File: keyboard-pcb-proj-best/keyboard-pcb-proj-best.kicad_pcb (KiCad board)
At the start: 2 copper layers, 24 parts, among them SW1 SW_PUSH, U1 ATmega32U4-A, Y1 16Mhz

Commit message: pcb routing
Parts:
- moved C4 1.73 mm to (94.0, 91.0)
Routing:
- net GND: track 65.5 -> 197.5 mm, vias 0 -> 2
- net +5V: track 44.0 -> 110.0 mm, vias 0 -> 7
- net ROW0: track 0.00 -> 20.4 mm
- net ROW1: track 0.00 -> 19.7 mm
- net COL1: track 0.00 -> 19.1 mm
- net COL0: track 0.00 -> 19.1 mm
- net Net-(D1-A): track 0.00 -> 7.17 mm
- net Net-(D2-A): track 0.00 -> 7.07 mm
- net Net-(D4-A): track 0.00 -> 7.00 mm
- net Net-(D3-A): track 0.00 -> 7.00 mm
- net Net-(U1-~{HWB}/PE2): track 0.00 -> 4.75 mm

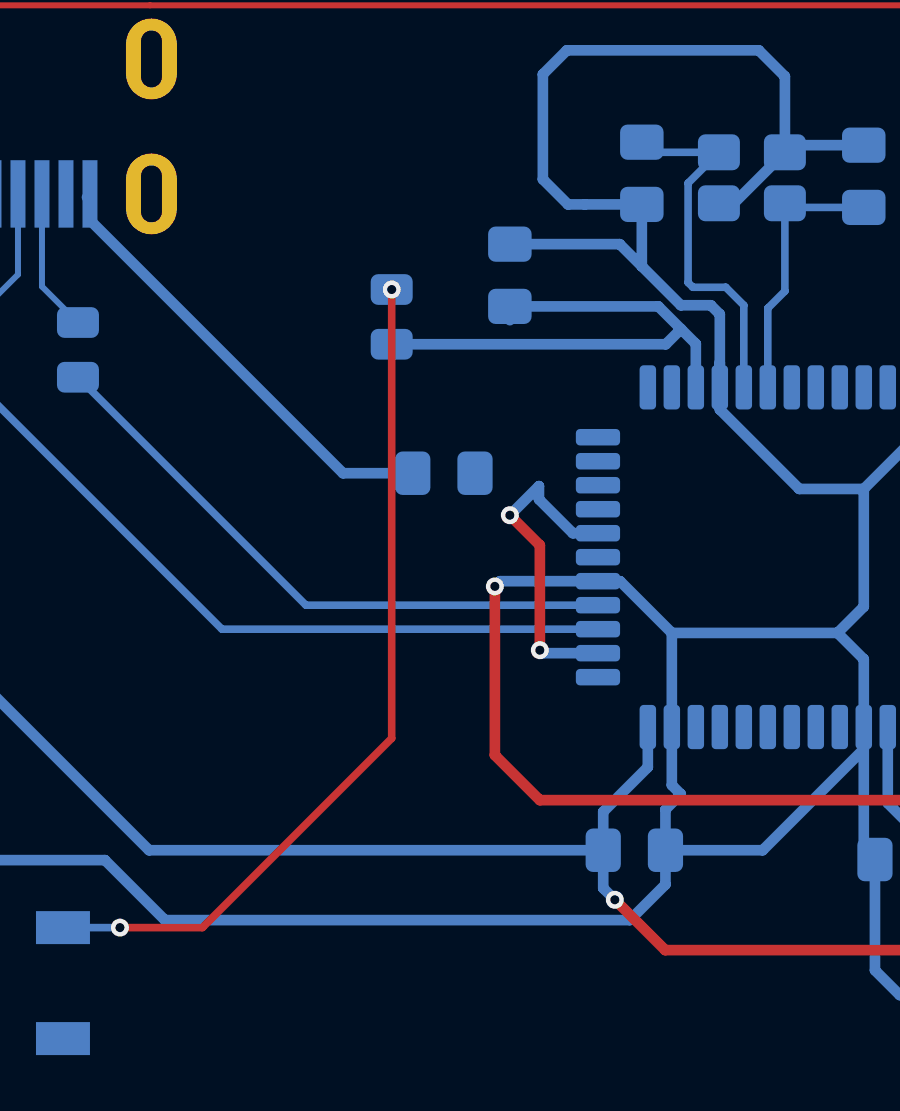
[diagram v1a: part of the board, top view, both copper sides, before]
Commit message: Finished Routing
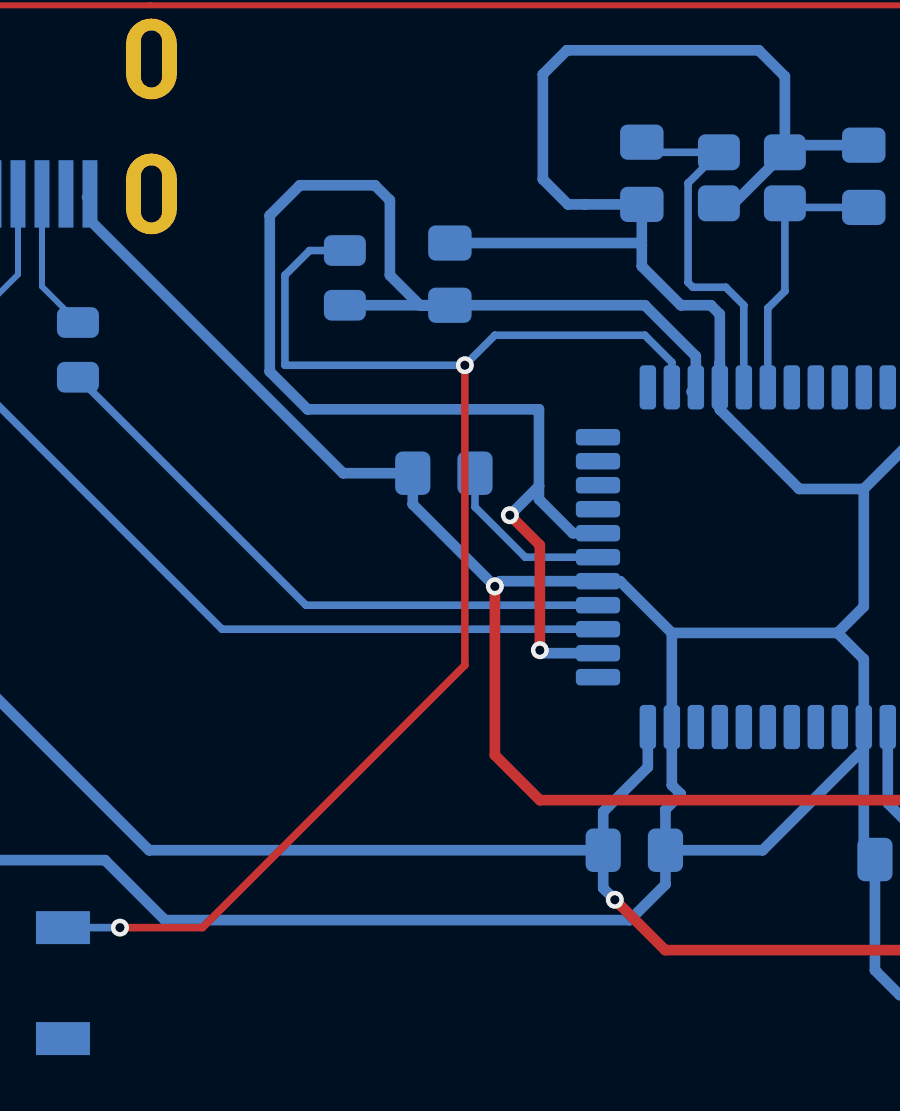
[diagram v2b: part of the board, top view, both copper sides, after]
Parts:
- moved R4 2.03 mm to (88.5, 91.1)
- moved C4 2.00 mm to (92.0, 91.0)
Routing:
- net +5V: track 110.0 -> 132.0 mm
- net Net-(U1-~{RESET}): track 29.1 -> 47.5 mm
- net GND: track 197.5 -> 204.1 mm
- net Net-(U1-UCAP): track 0.00 -> 5.92 mm
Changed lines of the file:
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@@
 	(footprint "Capacitor_SMD:C_0805_2012Metric_Pad1.18x1.45mm_HandSolder"
 		(layer "B.Cu")
-		(at 94 91 90)
+		(at 92 90.9625 90)
 		(descr "Capacitor SMD 0805 (2012 Metric), square (rectangular) end terminal, IPC-7351 nominal with elongated pad for handsoldering. (Body size source: IPC-SM-782 page 76, https://www.pcb-3d.com/wordpress/wp-content/uploads/ipc-sm-782a_amendment_1_and_2.pdf, https://docs.google.com/spreadsheets/d/1BsfQQcO9C6DZCsRaXUlFlo91Tg2WpOkGARC1WS5S8t0/edit?usp=sharing), generated with kicad-footprint-generator")
 		(tags "capacitor handsolder")
@@
 	(footprint "Resistor_SMD:R_0805_2012Metric"
 		(layer "B.Cu")
-		(at 90.06 92.3875 90)
+		(at 88.5 91.0875 90)
 		(descr "Resistor SMD 0805 (2012 Metric), square (rectangular) end terminal, IPC-7351 nominal, (Body size source: IPC-SM-782 page 72, https://www.pcb-3d.com/wordpress/wp-content/uploads/ipc-sm-782a_amendment_1_and_2.pdf), generated with kicad-footprint-generator")
 		(tags "resistor")
@@
 	)
 	(segment
+		(start 94.511873 100.4)
+		(end 96.9375 100.4)
+		(width 0.254)
+		(layer "B.Cu")
+		(net 1)
+	)
+	(segment
+		(start 92.8375 97.6)
+		(end 92.8375 98.725627)
+		(width 0.254)
+		(layer "B.Cu")
+		(net 1)
+	)
+	(segment
+		(start 92.8375 98.725627)
+		(end 94.511873 100.4)
+		(width 0.254)
+		(layer "B.Cu")
+		(net 1)
+	)
+	(segment
 		(start 93.5 107)
 		(end 95 108.5)
@@
 	)
 	(segment
+		(start 98.325 89.925)
+		(end 98.4 90)
+		(width 0.3556)
+		(layer "B.Cu")
+		(net 2)
+	)
+	(segment
 		(start 105.8 110.1075)
 		(end 105.8 106.0625)
@@
 	)
 	(segment
-		(start 97.6625 89.9625)
-		(end 98.4 90.7)
-		(width 0.3556)
-		(layer "B.Cu")
-		(net 2)
-	)
-	(segment
 		(start 99.7 92)
 		(end 100.7 92)
@@
 	)
 	(segment
+		(start 110.7625 96.4)
+		(end 108.2625 96.4)
+		(width 0.3556)
+		(layer "B.Cu")
+		(net 2)
+	)
+	(segment
 		(start 97.674999 101.2)
 		(end 96.9375 101.2)
@@
 	)
 	(segment
-		(start 112.91 94.2525)
-		(end 110.7625 96.4)
-		(width 0.3556)
-		(layer "B.Cu")
-		(net 2)
-	)
-	(segment
 		(start 98.4 90.7)
 		(end 99.7 92)
@@
 	)
 	(segment
-		(start 94 89.9625)
-		(end 97.6625 89.9625)
+		(start 90.7625 98.6355)
+		(end 93.5 101.373)
 		(width 0.3556)
 		(layer "B.Cu")
@@
 	)
 	(segment
-		(start 110.7625 96.4)
-		(end 108.2625 96.4)
-		(width 0.3556)
-		(layer "B.Cu")
-		(net 2)
-	)
-	(segment
 		(start 99.7 108.3)
 		(end 99.4 108)
@@
 	)
 	(segment
+		(start 90.7625 97.6)
+		(end 90.7625 98.6355)
+		(width 0.3556)
+		(layer "B.Cu")
+		(net 2)
+	)
+	(segment
 		(start 112.8 114.2)
 		(end 112.8 105.7125)
@@
 	)
 	(segment
+		(start 112.91 94.2525)
+		(end 110.7625 96.4)
+		(width 0.3556)
+		(layer "B.Cu")
+		(net 2)
+	)
+	(segment
 		(start 102.3 83.5)
 		(end 103.17 84.37)
@@
 	)
 	(segment
+		(start 98.4 90)
+		(end 98.4 90.7)
+		(width 0.3556)
+		(layer "B.Cu")
+		(net 2)
+	)
+	(segment
 		(start 72.9 116.45)
 		(end 71.45 116.45)
@@
 	)
 	(segment
+		(start 92 89.925)
+		(end 98.325 89.925)
+		(width 0.3556)
+		(layer "B.Cu")
+		(net 2)
+	)
+	(segment
 		(start 98.4 88.6375)
-		(end 98.4 90.7)
+		(end 98.4 90)
 		(width 0.3556)
 		(layer "B.Cu")
@@
 	)
 	(segment
-		(start 98.950348 92.0375)
-		(end 99.706424 92.793576)
+		(start 85.9942 89.0058)
+		(end 87 88)
+		(width 0.3556)
+		(layer "B.Cu")
+		(net 3)
+	)
+	(segment
+		(start 100.2 94.7375)
+		(end 100.0538 94.8837)
+		(width 0.3556)
+		(layer "B.Cu")
+		(net 3)
+	)
+	(segment
+		(start 87 88)
+		(end 89.5 88)
 		(width 0.3556)
 		(layer "B.Cu")
@@
 	)
 	(segment
+		(start 89.5 88)
+		(end 90 88.5)
+		(width 0.3556)
+		(layer "B.Cu")
+		(net 3)
+	)
+	(segment
+		(start 94.97 95.47)
+		(end 87.254691 95.47)
+		(width 0.3556)
+		(layer "B.Cu")
+		(net 3)
+	)
+	(segment
+		(start 100.2 93.7)
+		(end 98.5 92)
+		(width 0.3556)
+		(layer "B.Cu")
+		(net 3)
+	)
+	(segment
 		(start 108.2475 113.2525)
 		(end 108 113.5)
@@
 	)
 	(segment
-		(start 94 92.4975)
-		(end 94 92.0375)
+		(start 87.254691 95.47)
+		(end 85.9942 94.209509)
 		(width 0.3556)
 		(layer "B.Cu")
@@
 	)
 	(segment
-		(start 99.2 93.3)
-		(end 99.706424 92.793576)
+		(start 94.97 98.03)
+		(end 94.97 95.47)
+		(width 0.3556)
+		(layer "B.Cu")
+		(net 3)
+	)
+	(segment
+		(start 90 91)
+		(end 91 92)
 		(width 0.3556)
 		(layer "B.Cu")
@@
 	)
 	(segment
-		(start 99.706424 92.793576)
-		(end 100.2 93.287151)
+		(start 91 92)
+		(end 92 92)
 		(width 0.3556)
 		(layer "B.Cu")
@@
 	)
 	(segment
-		(start 94 99)
-		(end 94.97 98.03)
+		(start 100.2 94.7375)
+		(end 100.2 93.7)
 		(width 0.3556)
 		(layer "B.Cu")
@@
 	)
 	(segment
-		(start 94 92.0375)
-		(end 98.950348 92.0375)
+		(start 94 99)
+		(end 94.97 98.03)
 		(width 0.3556)
 		(layer "B.Cu")
@@
 	)
 	(segment
-		(start 100.2 93.287151)
-		(end 100.2 94.7375)
+		(start 85.9942 94.209509)
+		(end 85.9942 89.0058)
 		(width 0.3556)
 		(layer "B.Cu")
@@
 	)
 	(segment
+		(start 88.5 92)
+		(end 92 92)
+		(width 0.3556)
+		(layer "B.Cu")
+		(net 3)
+	)
+	(segment
+		(start 90 88.5)
+		(end 90 91)
+		(width 0.3556)
+		(layer "B.Cu")
+		(net 3)
+	)
+	(segment
 		(start 108.2475 110.48)
 		(end 108.2475 110.2475)
@@
 	)
 	(segment
-		(start 90.06 93.3)
-		(end 99.2 93.3)
+		(start 98.5 92)
+		(end 92 92)
 		(width 0.3556)
 		(layer "B.Cu")
@@
 	)
 	(segment
-		(start 83.75 112.75)
-		(end 90.06 106.44)
+		(start 92.5 104)
+		(end 92.5 94)
 		(width 0.254)
 		(layer "F.Cu")
@@
 	)
 	(segment
-		(start 90.06 106.44)
-		(end 90.06 91.475)
+		(start 81 112.75)
+		(end 83.75 112.75)
 		(width 0.254)
 		(layer "F.Cu")
@@
 	)
 	(segment
-		(start 81 112.75)
-		(end 83.75 112.75)
+		(start 83.75 112.75)
+		(end 92.5 104)
 		(width 0.254)
 		(layer "F.Cu")
@@
 	)
 	(via
-		(at 90.06 91.475)
+		(at 92.5 94)
 		(size 0.6)
 		(drill 0.3)
@@
 	)
 	(segment
+		(start 99.4 93.9)
+		(end 99.4 94.7375)
+		(width 0.254)
+		(layer "B.Cu")
+		(net 20)
+	)
+	(segment
 		(start 79.1 112.75)
 		(end 79.45 112.75)
@@
 	)
 	(segment
+		(start 93.5 93)
+		(end 98.5 93)
+		(width 0.254)
+		(layer "B.Cu")
+		(net 20)
+	)
+	(segment
+		(start 87.325 90.175)
+		(end 86.5 91)
+		(width 0.254)
+		(layer "B.Cu")
+		(net 20)
+	)
+	(segment
 		(start 79.45 112.75)
 		(end 79.6 112.9)
@@
 	)
 	(segment
+		(start 86.5 91)
+		(end 86.5 94)
+		(width 0.254)
+		(layer "B.Cu")
+		(net 20)
+	)
+	(segment
+		(start 86.5 94)
+		(end 92.5 94)
+		(width 0.254)
+		(layer "B.Cu")
+		(net 20)
+	)
+	(segment
+		(start 92.5 94)
+		(end 93.5 93)
+		(width 0.254)
+		(layer "B.Cu")
+		(net 20)
+	)
+	(segment
 		(start 81 112.75)
 		(end 79.1 112.75)
 		(width 0.254)
 		(layer "B.Cu")
+		(net 20)
+	)
+	(segment
+		(start 88.5 90.175)
+		(end 87.325 90.175)
+		(width 0.254)
+		(layer "B.Cu")
+		(net 20)
+	)
+	(segment
+		(start 98.5 93)
+		(end 99.4 93.9)
+		(width 0.254)
+		(layer "B.Cu")

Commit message: Minor Routing Changes
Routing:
- net GND: track 204.1 -> 205.1 mm
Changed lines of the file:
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@@
 	)
 	(gr_line
-		(start 82 120)
-		(end 70.2 120)
+		(start 81.9 120.5)
+		(end 70.1 120.5)
 		(stroke
 			(width 0.2)
@@
 	)
 	(gr_line
-		(start 68.2 118)
-		(end 68.2 84)
+		(start 154 84)
+		(end 154 118.5)
 		(stroke
 			(width 0.2)
@@
 	)
 	(gr_line
-		(start 154 84)
-		(end 154 118)
-		(stroke
-			(width 0.2)
-			(type default)
-		)
-		(layer "F.Cu")
-	)
-	(gr_line
-		(start 152 120)
-		(end 82 120)
+		(start 152 120.5)
+		(end 82 120.5)
 		(stroke
 			(width 0.2)
@@
 	)
 	(gr_arc
-		(start 70.2 120)
-		(mid 68.785786 119.414214)
-		(end 68.2 118)
+		(start 70.2 120.5)
+		(mid 68.785786 119.914214)
+		(end 68.2 118.5)
 		(stroke
 			(width 0.2)
@@
 	)
 	(gr_arc
-		(start 154 118)
-		(mid 153.414214 119.414214)
-		(end 152 120)
+		(start 154 118.5)
+		(mid 153.414214 119.914214)
+		(end 152 120.5)
+		(stroke
+			(width 0.2)
+			(type default)
+		)
+		(layer "F.Cu")
+	)
+	(gr_line
+		(start 68.2 84)
+		(end 68.2 118.5)
 		(stroke
 			(width 0.2)
@@
 	)
 	(segment
+		(start 92.8135 100.6865)
+		(end 93.5 101.373)
+		(width 0.3556)
+		(layer "B.Cu")
+		(net 2)
+	)
+	(segment
 		(start 105.8 86.6625)
 		(end 103.4075 86.6625)
@@
 	)
 	(segment
+		(start 94.596563 101.2)
+		(end 93.948281 100.551718)
+		(width 0.3556)
+		(layer "B.Cu")
+		(net 2)
+	)
+	(segment
 		(start 80 89.1625)
 		(end 88.4375 97.6)
@@
 	)
 	(segment
+		(start 93.948281 100.551718)
+		(end 93.813499 100.6865)
+		(width 0.3556)
+		(layer "B.Cu")
+		(net 2)
+	)
+	(segment
 		(start 105.8 103.8)
 		(end 104.925001 102.925001)
@@
 	)
 	(segment
-		(start 96.9375 101.2)
-		(end 93.673 101.2)
-		(width 0.3556)
-		(layer "B.Cu")
-		(net 2)
-	)
-	(segment
-		(start 93.673 101.2)
-		(end 93.5 101.373)
-		(width 0.3556)
-		(layer "B.Cu")
-		(net 2)
-	)
-	(segment
 		(start 112 115)
 		(end 112.8 114.2)
@@
 	(segment
 		(start 90.7625 98.6355)
-		(end 93.5 101.373)
+		(end 92.8135 100.6865)
 		(width 0.3556)
 		(layer "B.Cu")
@@
 	)
 	(segment
+		(start 93.813499 100.6865)
+		(end 92.8135 100.6865)
+		(width 0.3556)
+		(layer "B.Cu")
+		(net 2)
+	)
+	(segment
 		(start 72.9 116.45)
 		(end 71.45 116.45)
@@
 		(width 0.3556)
 		(layer "B.Cu")
+		(net 2)
+	)
+	(segment
+		(start 96.9375 101.2)
+		(end 94.596563 101.2)
+		(width 0.3556)
+		(layer "B.Cu")
